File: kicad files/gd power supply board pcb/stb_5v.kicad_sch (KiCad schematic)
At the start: 13 parts

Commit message: before erc
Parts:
- added H13, H14, H15, H16: MountingHole, MountingHole:MountingHole_2.2mm_M2, symbol Mechanical:MountingHole
- gave numbers to parts that had none: 13
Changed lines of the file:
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@@
     (effects (font (size 1.27 1.27)) (justify left))
   )
+  (symbol (lib_id "Mechanical:MountingHole") (at 215.9 52.07 0) (unit 1)
+    (in_bom yes) (on_board yes) (fields_autoplaced)
+    (property "Reference" "H13" (id 0) (at 218.44 50.7999 0)
+      (effects (font (size 1.27 1.27)) (justify left))
+    )
+    (property "Value" "MountingHole" (id 1) (at 218.44 53.3399 0)
+      (effects (font (size 1.27 1.27)) (justify left))
+    )
+    (property "Footprint" "MountingHole:MountingHole_2.2mm_M2" (id 2) (at 215.9 52.07 0)
+      (effects (font (size 1.27 1.27)) hide)
+    )
+    (property "Datasheet" "~" (id 3) (at 215.9 52.07 0)
+      (effects (font (size 1.27 1.27)) hide)
+    )
+  )
   (symbol (lib_id "power:GND") (at 186.69 97.028 0) (unit 1)
     (in_bom yes) (on_board yes)
-    (property "Reference" "#PWR?" (id 0) (at 186.69 103.378 0)
+    (property "Reference" "#PWR012" (id 0) (at 186.69 103.378 0)
       (effects (font (size 1.27 1.27)) hide)
     )
@@
   (symbol (lib_id "Device:C_Small") (at 156.21 80.264 0) (unit 1)
     (in_bom yes) (on_board yes)
-    (property "Reference" "C?" (id 0) (at 158.5468 79.0956 0)
+    (property "Reference" "C19" (id 0) (at 158.5468 79.0956 0)
       (effects (font (size 1.27 1.27)) (justify left))
     )
@@
   (symbol (lib_id "Device:L_Small") (at 166.37 88.9 90) (unit 1)
     (in_bom yes) (on_board yes)
-    (property "Reference" "L?" (id 0) (at 166.37 84.201 90))
+    (property "Reference" "L4" (id 0) (at 166.37 84.201 90))
     (property "Value" "1.5u" (id 1) (at 166.37 86.5124 90))
     (property "Footprint" "Inductor_SMD:L_Bourns_SRP5030T" (id 2) (at 166.37 88.9 0)
@@
     (pin "2")
   )
+  (symbol (lib_id "Mechanical:MountingHole") (at 224.79 52.07 0) (unit 1)
+    (in_bom yes) (on_board yes) (fields_autoplaced)
+    (property "Reference" "H15" (id 0) (at 227.33 50.7999 0)
+      (effects (font (size 1.27 1.27)) (justify left))
+    )
+    (property "Value" "MountingHole" (id 1) (at 227.33 53.3399 0)
+      (effects (font (size 1.27 1.27)) (justify left))
+    )
+    (property "Footprint" "MountingHole:MountingHole_2.2mm_M2" (id 2) (at 224.79 52.07 0)
+      (effects (font (size 1.27 1.27)) hide)
+    )
+    (property "Datasheet" "~" (id 3) (at 224.79 52.07 0)
+      (effects (font (size 1.27 1.27)) hide)
+    )
+  )
   (symbol (lib_id "Device:R_Small") (at 172.72 92.202 180) (unit 1)
     (in_bom yes) (on_board yes)
-    (property "Reference" "R?" (id 0) (at 174.2186 91.0336 0)
+    (property "Reference" "R24" (id 0) (at 174.2186 91.0336 0)
       (effects (font (size 1.27 1.27)) (justify right))
     )
@@
   (symbol (lib_id "My Library:TestPoint_Harwin") (at 160.02 93.98 180) (unit 1)
     (in_bom yes) (on_board yes) (fields_autoplaced)
-    (property "Reference" "TP?" (id 0) (at 162.56 97.2819 0)
+    (property "Reference" "TP28" (id 0) (at 162.56 97.2819 0)
       (effects (font (size 1.27 1.27)) (justify right))
     )
@@
   (symbol (lib_id "Device:C_Small") (at 186.69 92.71 0) (unit 1)
     (in_bom yes) (on_board yes)
-    (property "Reference" "C?" (id 0) (at 189.0268 91.5416 0)
+    (property "Reference" "C20" (id 0) (at 189.0268 91.5416 0)
       (effects (font (size 1.27 1.27)) (justify left))
     )
@@
   (symbol (lib_id "power:GND") (at 196.85 96.774 0) (unit 1)
     (in_bom yes) (on_board yes)
-    (property "Reference" "#PWR?" (id 0) (at 196.85 103.124 0)
+    (property "Reference" "#PWR013" (id 0) (at 196.85 103.124 0)
       (effects (font (size 1.27 1.27)) hide)
     )
@@
   (symbol (lib_id "power:GND") (at 172.72 104.648 0) (unit 1)
     (in_bom yes) (on_board yes)
-    (property "Reference" "#PWR?" (id 0) (at 172.72 110.998 0)
+    (property "Reference" "#PWR011" (id 0) (at 172.72 110.998 0)
       (effects (font (size 1.27 1.27)) hide)
     )
@@
   (symbol (lib_id "My Library:TestPoint_Harwin") (at 172.72 88.9 0) (unit 1)
     (in_bom yes) (on_board yes)
-    (property "Reference" "TP?" (id 0) (at 171.45 83.82 0)
+    (property "Reference" "TP29" (id 0) (at 171.45 83.82 0)
       (effects (font (size 1.27 1.27)) (justify left))
     )
@@
   (symbol (lib_id "TO3-Switching-Supply-rescue:TPS563200-Regulator_Switching") (at 138.43 91.44 0) (unit 1)
     (in_bom yes) (on_board yes)
-    (property "Reference" "U?" (id 0) (at 138.43 82.1182 0))
+    (property "Reference" "U4" (id 0) (at 138.43 82.1182 0))
     (property "Value" "TPS563240DDCR" (id 1) (at 138.43 84.4296 0))
     (property "Footprint" "Package_TO_SOT_SMD:SOT-23-6" (id 2) (at 139.7 97.79 0)
@@
   (symbol (lib_id "Device:R_Small") (at 172.72 100.33 180) (unit 1)
     (in_bom yes) (on_board yes)
-    (property "Reference" "R?" (id 0) (at 174.2186 99.1616 0)
+    (property "Reference" "R25" (id 0) (at 174.2186 99.1616 0)
       (effects (font (size 1.27 1.27)) (justify right))
     )
@@
   (symbol (lib_id "Device:C_Small") (at 110.49 93.98 0) (unit 1)
     (in_bom yes) (on_board yes)
-    (property "Reference" "C?" (id 0) (at 112.8268 92.8116 0)
+    (property "Reference" "C18" (id 0) (at 112.8268 92.8116 0)
       (effects (font (size 1.27 1.27)) (justify left))
     )
@@
   (symbol (lib_id "power:GND") (at 101.6 97.79 0) (unit 1)
     (in_bom yes) (on_board yes)
-    (property "Reference" "#PWR?" (id 0) (at 101.6 104.14 0)
+    (property "Reference" "#PWR08" (id 0) (at 101.6 104.14 0)
       (effects (font (size 1.27 1.27)) hide)
     )
@@
   (symbol (lib_id "power:GND") (at 138.43 101.6 0) (unit 1)
     (in_bom yes) (on_board yes)
-    (property "Reference" "#PWR?" (id 0) (at 138.43 107.95 0)
+    (property "Reference" "#PWR010" (id 0) (at 138.43 107.95 0)
       (effects (font (size 1.27 1.27)) hide)
     )
@@
   (symbol (lib_id "power:GND") (at 110.49 97.79 0) (unit 1)
     (in_bom yes) (on_board yes)
-    (property "Reference" "#PWR?" (id 0) (at 110.49 104.14 0)
+    (property "Reference" "#PWR09" (id 0) (at 110.49 104.14 0)
       (effects (font (size 1.27 1.27)) hide)
     )
@@
   (symbol (lib_id "Device:C_Small") (at 196.85 92.456 0) (unit 1)
     (in_bom yes) (on_board yes)
-    (property "Reference" "C?" (id 0) (at 199.1868 91.2876 0)
+    (property "Reference" "C21" (id 0) (at 199.1868 91.2876 0)
       (effects (font (size 1.27 1.27)) (justify left))
     )
@@
     (pin "2")
   )
+  (symbol (lib_id "Mechanical:MountingHole") (at 215.9 58.42 0) (unit 1)
+    (in_bom yes) (on_board yes) (fields_autoplaced)
+    (property "Reference" "H14" (id 0) (at 218.44 57.1499 0)
+      (effects (font (size 1.27 1.27)) (justify left))
+    )
+    (property "Value" "MountingHole" (id 1) (at 218.44 59.6899 0)
+      (effects (font (size 1.27 1.27)) (justify left))
+    )
+    (property "Footprint" "MountingHole:MountingHole_2.2mm_M2" (id 2) (at 215.9 58.42 0)
+      (effects (font (size 1.27 1.27)) hide)
+    )
+    (property "Datasheet" "~" (id 3) (at 215.9 58.42 0)
+      (effects (font (size 1.27 1.27)) hide)
+    )
+  )
   (symbol (lib_id "Device:C_Small") (at 101.6 92.71 0) (unit 1)
     (in_bom yes) (on_board yes)
-    (property "Reference" "C?" (id 0) (at 103.9368 91.5416 0)
+    (property "Reference" "C17" (id 0) (at 103.9368 91.5416 0)
       (effects (font (size 1.27 1.27)) (justify left))
     )
@@
   (symbol (lib_id "My Library:TestPoint_Harwin") (at 110.49 88.9 0) (unit 1)
     (in_bom yes) (on_board yes)
-    (property "Reference" "TP?" (id 0) (at 109.22 83.82 0)
+    (property "Reference" "TP26" (id 0) (at 109.22 83.82 0)
       (effects (font (size 1.27 1.27)) (justify left))
     )
@@
     (pin "1")
   )
+  (symbol (lib_id "Mechanical:MountingHole") (at 224.79 58.42 0) (unit 1)
+    (in_bom yes) (on_board yes) (fields_autoplaced)
+    (property "Reference" "H16" (id 0) (at 227.33 57.1499 0)
+      (effects (font (size 1.27 1.27)) (justify left))
+    )
+    (property "Value" "MountingHole" (id 1) (at 227.33 59.6899 0)
+      (effects (font (size 1.27 1.27)) (justify left))
+    )
+    (property "Footprint" "MountingHole:MountingHole_2.2mm_M2" (id 2) (at 224.79 58.42 0)
+      (effects (font (size 1.27 1.27)) hide)
+    )
+    (property "Datasheet" "~" (id 3) (at 224.79 58.42 0)
+      (effects (font (size 1.27 1.27)) hide)
+    )
+  )
   (symbol (lib_id "My Library:TestPoint_Harwin") (at 160.02 88.9 0) (unit 1)
     (in_bom yes) (on_board yes)
-    (property "Reference" "TP?" (id 0) (at 158.75 83.82 0)
-      (effects (font (size 1.27 1.27)) (justify left))
-    )
+    (property "Reference" "TP27" (id 0) (at 158.75 83.82 0)
+      (effects (font (size 1.27 1.27)) (justify left))
+    )

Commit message: minor fixes and compacting the floorplan. stacked 5V supplies for maximum minimage.
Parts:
- removed H13, H14, H15, H16: MountingHole, MountingHole:MountingHole_2.2mm_M2, symbol Mechanical:MountingHole
- removed TP26: TestPoint_Harwin, My Libraries:Harwin-S1751-46-Test-Point, symbol My Library:TestPoint_Harwin
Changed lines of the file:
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@@
     (effects (font (size 1.27 1.27)) (justify left))
-  )
-  (symbol (lib_id "Mechanical:MountingHole") (at 215.9 52.07 0) (unit 1)
-    (in_bom yes) (on_board yes) (fields_autoplaced)
-    (property "Reference" "H13" (id 0) (at 218.44 50.7999 0)
-      (effects (font (size 1.27 1.27)) (justify left))
-    )
-    (property "Value" "MountingHole" (id 1) (at 218.44 53.3399 0)
-      (effects (font (size 1.27 1.27)) (justify left))
-    )
-    (property "Footprint" "MountingHole:MountingHole_2.2mm_M2" (id 2) (at 215.9 52.07 0)
-      (effects (font (size 1.27 1.27)) hide)
-    )
-    (property "Datasheet" "~" (id 3) (at 215.9 52.07 0)
-      (effects (font (size 1.27 1.27)) hide)
-    )
   )
   (symbol (lib_id "power:GND") (at 186.69 97.028 0) (unit 1)
@@
     (pin "1")
     (pin "2")
-  )
-  (symbol (lib_id "Mechanical:MountingHole") (at 224.79 52.07 0) (unit 1)
-    (in_bom yes) (on_board yes) (fields_autoplaced)
-    (property "Reference" "H15" (id 0) (at 227.33 50.7999 0)
-      (effects (font (size 1.27 1.27)) (justify left))
-    )
-    (property "Value" "MountingHole" (id 1) (at 227.33 53.3399 0)
-      (effects (font (size 1.27 1.27)) (justify left))
-    )
-    (property "Footprint" "MountingHole:MountingHole_2.2mm_M2" (id 2) (at 224.79 52.07 0)
-      (effects (font (size 1.27 1.27)) hide)
-    )
-    (property "Datasheet" "~" (id 3) (at 224.79 52.07 0)
-      (effects (font (size 1.27 1.27)) hide)
-    )
   )
   (symbol (lib_id "Device:R_Small") (at 172.72 92.202 180) (unit 1)
@@
     (pin "2")
   )
-  (symbol (lib_id "Mechanical:MountingHole") (at 215.9 58.42 0) (unit 1)
-    (in_bom yes) (on_board yes) (fields_autoplaced)
-    (property "Reference" "H14" (id 0) (at 218.44 57.1499 0)
-      (effects (font (size 1.27 1.27)) (justify left))
-    )
-    (property "Value" "MountingHole" (id 1) (at 218.44 59.6899 0)
-      (effects (font (size 1.27 1.27)) (justify left))
-    )
-    (property "Footprint" "MountingHole:MountingHole_2.2mm_M2" (id 2) (at 215.9 58.42 0)
-      (effects (font (size 1.27 1.27)) hide)
-    )
-    (property "Datasheet" "~" (id 3) (at 215.9 58.42 0)
-      (effects (font (size 1.27 1.27)) hide)
-    )
-  )
   (symbol (lib_id "Device:C_Small") (at 101.6 92.71 0) (unit 1)
     (in_bom yes) (on_board yes)
@@
     (pin "2")
   )
-  (symbol (lib_id "My Library:TestPoint_Harwin") (at 110.49 88.9 0) (unit 1)
-    (in_bom yes) (on_board yes)
-    (property "Reference" "TP26" (id 0) (at 109.22 83.82 0)
-      (effects (font (size 1.27 1.27)) (justify left))
-    )
-    (property "Value" "TestPoint_Harwin" (id 1) (at 110.49 83.82 0)
-      (effects (font (size 1.27 1.27)) hide)
-    )
-    (property "Footprint" "My Libraries:Harwin-S1751-46-Test-Point" (id 2) (at 115.57 88.9 0)
-      (effects (font (size 1.27 1.27)) hide)
-    )
-    (property "Datasheet" "~" (id 3) (at 115.57 88.9 0)
-      (effects (font (size 1.27 1.27)) hide)
-    )
-    (pin "1")
-  )
-  (symbol (lib_id "Mechanical:MountingHole") (at 224.79 58.42 0) (unit 1)
-    (in_bom yes) (on_board yes) (fields_autoplaced)
-    (property "Reference" "H16" (id 0) (at 227.33 57.1499 0)
-      (effects (font (size 1.27 1.27)) (justify left))
-    )
-    (property "Value" "MountingHole" (id 1) (at 227.33 59.6899 0)
-      (effects (font (size 1.27 1.27)) (justify left))
-    )
-    (property "Footprint" "MountingHole:MountingHole_2.2mm_M2" (id 2) (at 224.79 58.42 0)
-      (effects (font (size 1.27 1.27)) hide)
-    )
-    (property "Datasheet" "~" (id 3) (at 224.79 58.42 0)
-      (effects (font (size 1.27 1.27)) hide)
-    )
-  )
   (symbol (lib_id "My Library:TestPoint_Harwin") (at 160.02 88.9 0) (unit 1)

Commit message: pre-routing try 1
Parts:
- added JP5: stb_5v_jmp, Jumper:SolderJumper-2_P1.3mm_Open_TrianglePad1.0x1.5mm, symbol Jumper:Jumper_2_Open
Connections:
- net Vin: now also JP5.1 (A); no longer C17.1, C18.1, U4.3 (VIN), U4.5 (EN)
- new net stb_Vin: C17.1, C18.1, JP5.2 (B), U4.3 (VIN), U4.5 (EN)
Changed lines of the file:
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@@
     (stroke (width 0) (type default) (color 0 0 0 0))
   )
-  (wire (pts (xy 97.79 88.9) (xy 101.6 88.9))
+  (wire (pts (xy 91.44 88.9) (xy 101.6 88.9))
     (stroke (width 0) (type default) (color 0 0 0 0))
   )
@@
   )
   (wire (pts (xy 160.02 88.9) (xy 163.83 88.9))
+    (stroke (width 0) (type default) (color 0 0 0 0))
+  )
+  (wire (pts (xy 78.74 88.9) (xy 81.28 88.9))
     (stroke (width 0) (type default) (color 0 0 0 0))
   )
@@
     (effects (font (size 1.27 1.27)) (justify right bottom))
   )
-  (label "Vin" (at 102.87 88.9 0)
+  (label "stb_Vin" (at 101.6 88.9 0)
     (effects (font (size 1.27 1.27)) (justify left bottom))
-  )
-  (hierarchical_label "Vin" (shape input) (at 97.79 88.9 180)
-    (effects (font (size 1.27 1.27)) (justify right))
   )
   (hierarchical_label "stb_5v" (shape input) (at 200.66 88.9 0)
     (effects (font (size 1.27 1.27)) (justify left))
+  )
+  (hierarchical_label "Vin" (shape input) (at 78.74 88.9 180)
+    (effects (font (size 1.27 1.27)) (justify right))
   )
   (symbol (lib_id "power:GND") (at 186.69 97.028 0) (unit 1)
@@
       (effects (font (size 1.27 1.27)) hide)
     )
+    (pin "1")
+    (pin "2")
+  )
+  (symbol (lib_id "Jumper:Jumper_2_Open") (at 86.36 88.9 0) (unit 1)
+    (in_bom yes) (on_board yes) (fields_autoplaced)
+    (property "Reference" "JP5" (id 0) (at 86.36 82.55 0))
+    (property "Value" "stb_5v_jmp" (id 1) (at 86.36 85.09 0))
+    (property "Footprint" "Jumper:SolderJumper-2_P1.3mm_Open_TrianglePad1.0x1.5mm" (id 2) (at 86.36 88.9 0)
+      (effects (font (size 1.27 1.27)) hide)
+    )
+    (property "Datasheet" "~" (id 3) (at 86.36 88.9 0)
+      (effects (font (size 1.27 1.27)) hide)
+    )

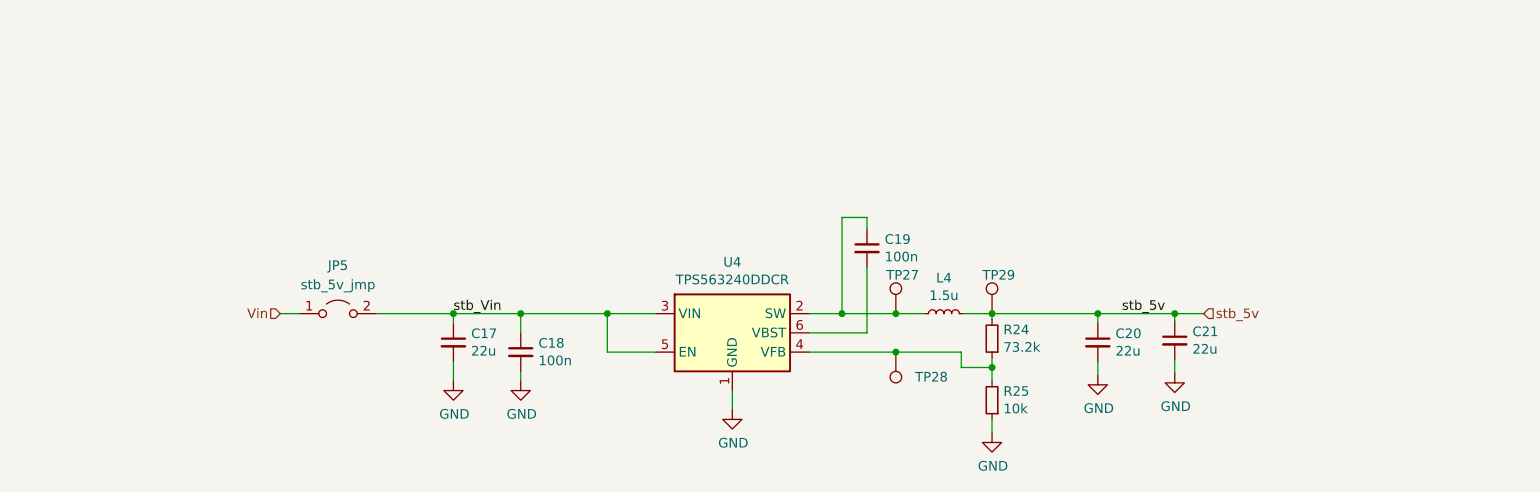
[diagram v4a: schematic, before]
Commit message: added filters and ripped up the board
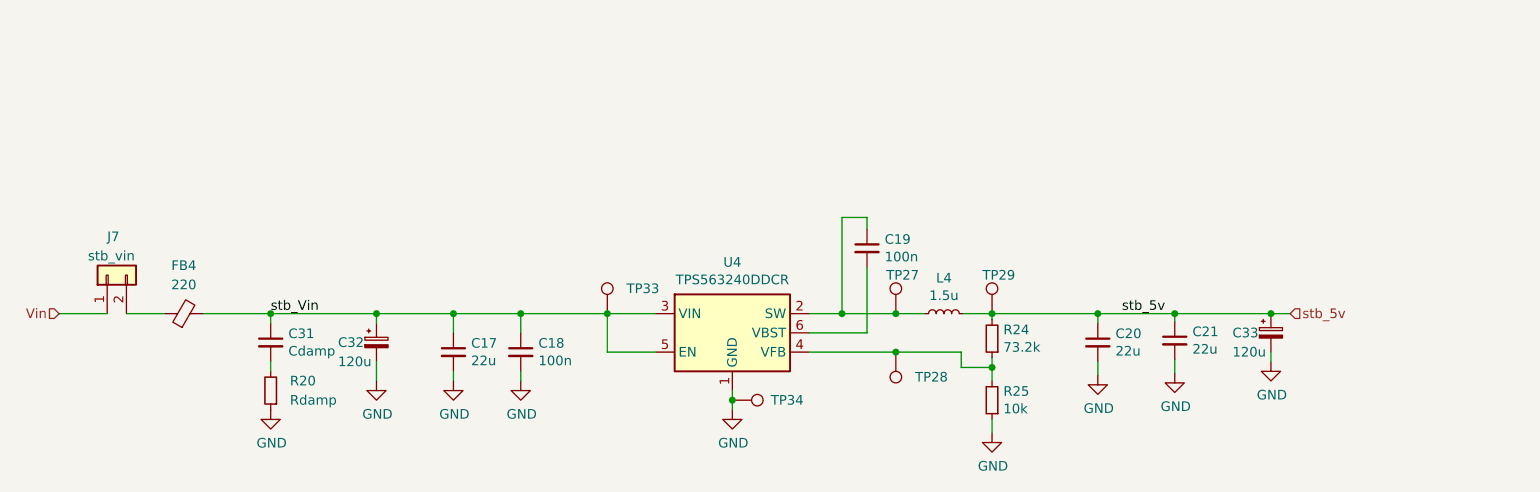
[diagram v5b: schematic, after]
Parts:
- removed JP5: stb_5v_jmp, Jumper:SolderJumper-2_P1.3mm_Open_TrianglePad1.0x1.5mm, symbol Jumper:Jumper_2_Open
- added C31: Cdamp, Capacitor_SMD:C_0805_2012Metric_Pad1.18x1.45mm_HandSolder, symbol Device:C_Small
- added C32, C33: 120u, Capacitor_THT:CP_Radial_D8.0mm_P3.80mm, symbol Device:C_Polarized_Small
- added FB4: 220, Inductor_SMD:L_0603_1608Metric_Pad1.05x0.95mm_HandSolder, symbol Device:FerriteBead_Small
- added J7: stb_vin, Connector_PinHeader_2.54mm:PinHeader_1x02_P2.54mm_Vertical, symbol Connector_Generic:Conn_01x02
- added R20: Rdamp, Resistor_SMD:R_0805_2012Metric_Pad1.20x1.40mm_HandSolder, symbol My Library:R_0805
- added TP33: TestPoint_Harwin, My Libraries:Harwin-S1751-46-Test-Point, symbol My Library:TestPoint_Harwin
- added TP34: TestPoint_Harwin, TestPoint:TestPoint_Pad_1.0x1.0mm, symbol My Library:TestPoint_Harwin
- C17: footprint Capacitor_SMD:C_0805_2012Metric -> Capacitor_SMD:C_0805_2012Metric_Pad1.18x1.45mm_HandSolder
- C18: footprint Capacitor_SMD:C_0603_1608Metric -> Capacitor_SMD:C_0603_1608Metric_Pad1.08x0.95mm_HandSolder
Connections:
- net GND: now also C32.2, C33.2, R20.1, TP34.1
- net Vin: now also J7.1 (Pin_1)
- net stb_5v: now also C33.1
- net stb_Vin: now also C31.1, C32.1, FB4.2, TP33.1
- new net: FB4.1, J7.2 (Pin_2)
- new net: C31.2, R20.2
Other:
- moved on the sheet: C17

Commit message: rev2 - round 1
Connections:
- net stb_FB: now reaches R24.1, R25.2, TP28.1, U4.4 (VFB)
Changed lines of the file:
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@@
+    (effects (font (size 1.27 1.27)) (justify left bottom))
+  )
+  (label "stb_FB" (at 151.13 93.98 0)
+    (effects (font (size 1.27 1.27)) (justify left bottom))
+  )
+  (label "stb_SW" (at 152.4 76.2 0)
     (effects (font (size 1.27 1.27)) (justify left bottom))
   )

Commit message: Updated title blocks for rev2
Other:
- company: (none) -> twitch.tv/baldengineer
- title: (none) -> GD Power Supply Prototype
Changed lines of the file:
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@@
 (kicad_sch (version 20211123) (generator eeschema)
   (paper "A4")
+  (title_block
+    (title "GD Power Supply Prototype")
+    (date "2022-05-16")
+    (rev "Rev 2")
+    (company "twitch.tv/baldengineer")
+  )
   (junction (at 160.02 93.98) (diameter 0) (color 0 0 0 0)
   )
